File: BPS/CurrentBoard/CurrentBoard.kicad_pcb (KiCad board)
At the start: 2 copper layers, 30 parts, among them J1 ShuntConn, J2 LeaderConn, U1 AS8510-ASSM, U2 RO-123.3S_HP, U3 LTC6820, U4 HX1188FNL

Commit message: Organizes and edits PCB layout
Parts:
- C6, C7, C8, C9: moved to B.Cu
- moved R1 75.3 mm to (109.3, 135.2), turned to 180 degrees
- moved C7 68.8 mm to (111.7, 131.1), turned to 270 degrees
- moved J2 58.8 mm to (168.0, 135.5), turned to 90 degrees
- moved J1 53.9 mm to (102.2, 126.5), turned to 270 degrees
- moved C6 51.8 mm to (123.9, 131.1), turned to 270 degrees
- moved R3 51.7 mm to (125.1, 127.0)
- moved C2 49.3 mm to (109.3, 131.8), turned to 180 degrees
- moved U1 48.9 mm to (117.8, 136.0)
- moved U4 46.4 mm to (153.2, 130.0)
- moved U3 45.4 mm to (189.0, 101.5)
- moved C5 42.1 mm to (137.6, 102.0)
- moved C1 41.1 mm to (131.5, 106.0)
- moved TP1 41.0 mm to (124.5, 91.0)
- moved R4 35.6 mm to (150.2, 138.0)
- moved TP3 35.6 mm to (124.5, 106.0)
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
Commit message: Worked on layout of board
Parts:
- removed TP2: GNDPWR_TP, TestPoint:TestPoint_Keystone_5005-5009_Compact
- added GNDPWR: GNDPWR_TP, TestPoint:TestPoint_Keystone_5005-5009_Compact, F.Cu at (125.6, 110.0)
- C1, C2, C4: moved to B.Cu
- moved H4 77.5 mm to (102.9, 126.4)
- moved R5 69.1 mm to (130.5, 122.8), turned to 180 degrees
- moved C8 68.3 mm to (126.7, 127.7)
- moved C9 67.3 mm to (131.1, 127.8)
- moved R6 67.3 mm to (132.1, 125.5)
- moved U3 67.3 mm to (126.6, 126.8)
- moved H1 64.7 mm to (102.9, 111.8)
- moved H2 32.3 mm to (160.7, 111.8)
- moved H3 30.8 mm to (160.7, 127.0)
- moved J2 29.0 mm to (152.9, 110.7), turned to 180 degrees
- moved J1 23.7 mm to (119.6, 110.4), turned to 180 degrees
- moved U2 21.9 mm to (130.6, 118.6)
- moved C5 21.2 mm to (123.3, 117.7), turned to 270 degrees
- moved R1 20.5 mm to (110.2, 114.8), turned to 90 degrees
- moved 12V 19.6 mm to (129.8, 109.9)
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- renumbered TP1 to 12V, TP3 to 3.3V, TP4 to GND
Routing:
- net GND: track 0.00 -> 71.2 mm, vias 0 -> 5
- net +3V3: track 0.00 -> 57.9 mm, vias 0 -> 5
- net +12V: track 0.00 -> 42.0 mm
- net GNDPWR: track 0.00 -> 41.5 mm
- net /IM: track 0.00 -> 21.7 mm
- net /IP: track 0.00 -> 19.9 mm
- net /SCK: track 0.00 -> 14.7 mm
- net /CS: track 0.00 -> 14.0 mm
- net /MISO: track 0.00 -> 12.3 mm
- net /MOSI: track 0.00 -> 8.73 mm
- net Net-(J2-Pad2): track 0.00 -> 7.37 mm, vias 0 -> 1
- net Net-(R1-Pad1): track 0.00 -> 5.94 mm
- net Net-(R5-Pad1): track 0.00 -> 5.80 mm
- net /RSHL: track 0.00 -> 5.74 mm
- net /RSHH: track 0.00 -> 5.65 mm
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
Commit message: Finishes PCB layout of current board
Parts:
- added G***: LOGO, UTSVT_Special:Hallock_Image_Tiny, B.Cu at (131.5, 116.2)
- added G***: LOGO, UTSVT_Special:UTSVT_Logo_Symbol, F.Cu at (131.0, 101.0)
- C2, C4: moved to F.Cu
- moved TP3 39.3 mm to (99.1, 103.3), turned to 90 degrees
- moved R2 38.8 mm to (103.1, 104.3)
- moved TP4 34.8 mm to (99.1, 109.7), turned to 90 degrees
- moved D1 34.6 mm to (103.1, 108.7), turned to 90 degrees
- moved J1 29.1 mm to (91.2, 116.6), turned to 90 degrees
- moved U2 25.2 mm to (110.5, 103.4), turned to 180 degrees
- moved C3 25.1 mm to (113.0, 99.8), turned to 0 degrees
- moved R4 24.8 mm to (121.7, 119.6), turned to 270 degrees
- moved C5 22.8 mm to (109.1, 99.8), turned to 180 degrees
- moved H2 21.2 mm to (143.0, 100.0)
- moved C4 19.5 mm to (99.7, 114.9), turned to 0 degrees
- moved C1 18.1 mm to (113.0, 107.9), turned to 0 degrees
- moved U4 18.1 mm to (131.2, 113.6), turned to 270 degrees
- moved H3 17.9 mm to (143.0, 124.2)
- moved H1 16.9 mm to (90.8, 100.0)
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- renumbered 12V to TP1, GNDPWR to TP2, 3.3V to TP3, GND to TP4
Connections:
- J1 pad 1: /RSHH -> /ETS
- J1 pad 3: /ETS -> /RSHH
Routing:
- net GND: track 71.2 -> 25.8 mm
- net +3V3: track 57.9 -> 45.9 mm, vias 5 -> 4
- net /SCK: track 14.7 -> 4.35 mm
- net /CS: track 14.0 -> 4.41 mm
- net /RSHH: track 5.65 -> 14.8 mm, vias 0 -> 1
- net /ETS: track 5.36 -> 14.1 mm, vias 0 -> 1
- net /MISO: track 12.3 -> 4.29 mm
- net /RSHL: track 5.74 -> 13.1 mm, vias 0 -> 1
- net /IM: track 21.7 -> 15.6 mm
- net /MOSI: track 8.73 -> 4.03 mm
- net Net-(J2-Pad3): track 3.97 -> 8.30 mm
- net GNDPWR: track 41.5 -> 45.6 mm
- net /IP: track 19.9 -> 16.1 mm
- net Net-(D1-Pad2): track 0.00 -> 2.60 mm
- net +12V: track 42.0 -> 43.3 mm
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- added copper zone on F.Cu, net GND
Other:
- board outline added: 58.2 x 30.2 mm
- net class Default: clearance 0.2 -> 0.127
- rule trace_clearance: 0.2 -> 0.127
- board text added: "+12V"
- board text added: "+3.3V"
- board text added: "Dr. Gary Hallock"
- board text added: "ETS"
- board text added: "GND"
- board text added: "GND PWR"
- board text added: "GNDPWR"
- board text added: "Hannah was here"
- board text added: "IM"
- board text added: "IP"
- board text added: "RSHH"
- board text added: "RSHL"
- board text added: "UTSVT - BPS Current Board v2.0 Summer 2020"

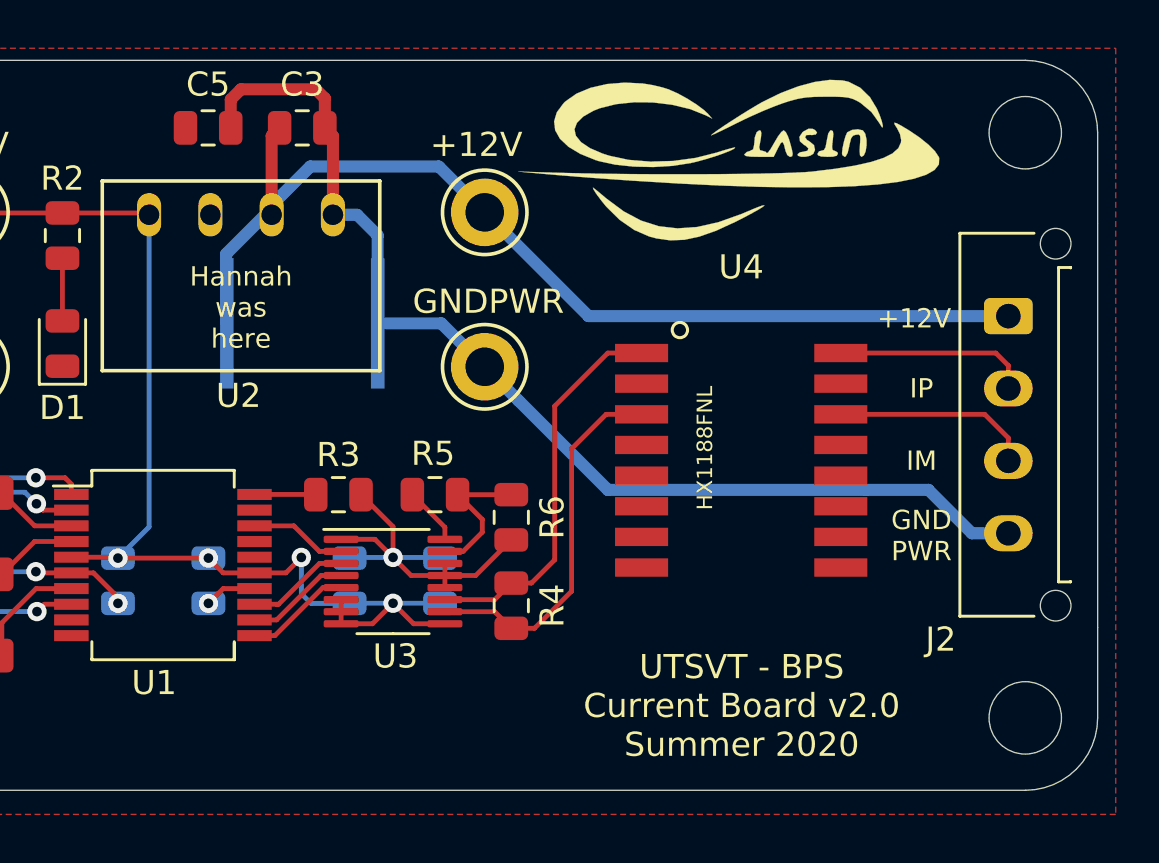
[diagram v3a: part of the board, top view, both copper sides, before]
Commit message: Adds keepout zone for the transformer and the dimensions
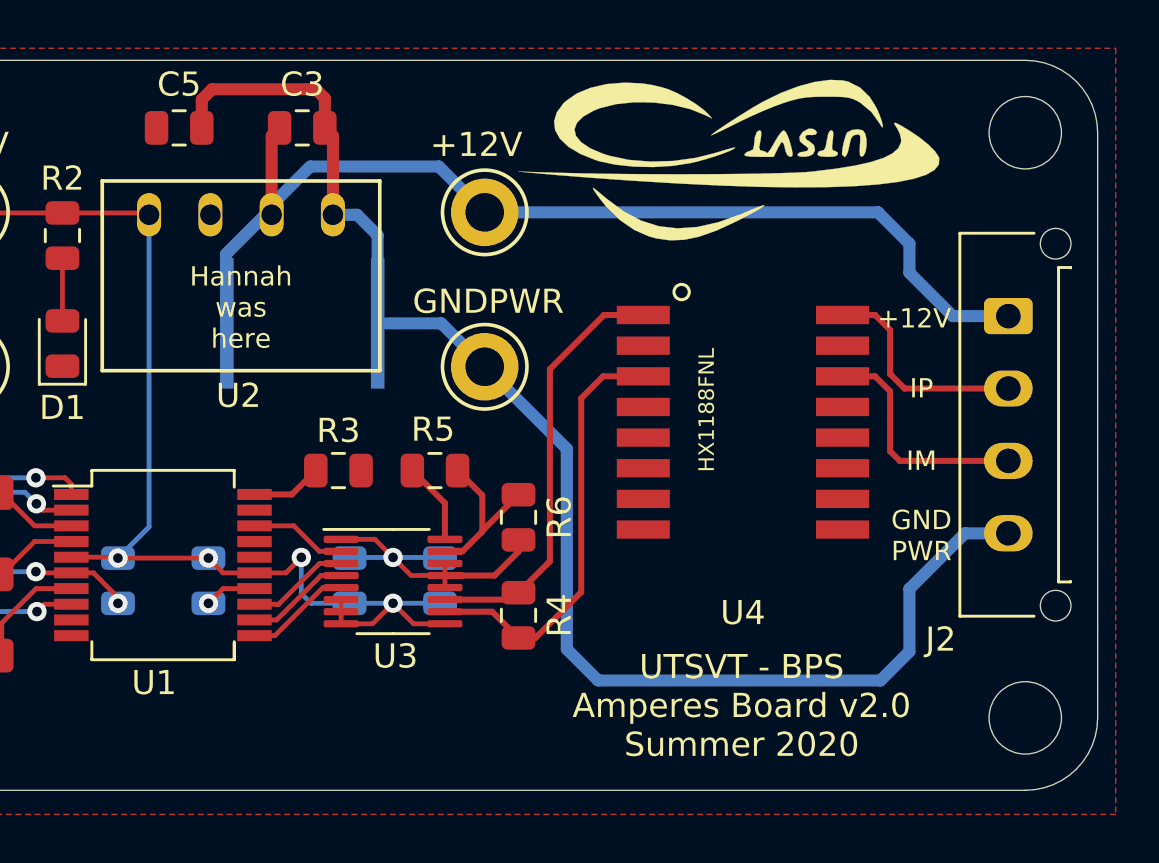
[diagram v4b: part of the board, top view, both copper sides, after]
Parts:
- moved G*** 3.15 mm to (131.6, 113.1)
- moved U4 1.58 mm to (131.3, 112.0)
- moved C5 1.20 mm to (107.9, 99.8)
- moved R3 1.00 mm to (114.5, 114.0)
- moved R5 1.00 mm to (118.5, 114.0)
- moved R4 0.50 mm to (122.0, 120.0)
- moved R6 0.30 mm to (122.0, 115.9)
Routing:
- net GNDPWR: track 45.6 -> 58.2 mm
- net GND: track 25.8 -> 23.2 mm
- net /IM: track 15.6 -> 17.9 mm
- net /IP: track 16.1 -> 17.8 mm
- net Net-(J2-Pad3): track 8.30 -> 9.78 mm
- net Net-(J2-Pad2): track 8.11 -> 9.20 mm
- net Net-(R5-Pad2): track 2.41 -> 3.41 mm
- net Net-(R5-Pad1): track 6.08 -> 6.99 mm
- net +12V: track 43.3 -> 44.0 mm
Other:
- board text added: "UTSVT - BPS Amperes Board v2.0 Summer 2020"
- board text removed: "UTSVT - BPS Current Board v2.0 Summer 2020"
